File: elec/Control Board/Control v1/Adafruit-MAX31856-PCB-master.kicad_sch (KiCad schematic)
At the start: 23 parts, among them U1 mic5225-3.3, U2 MAX31856, X1 3.5mm term

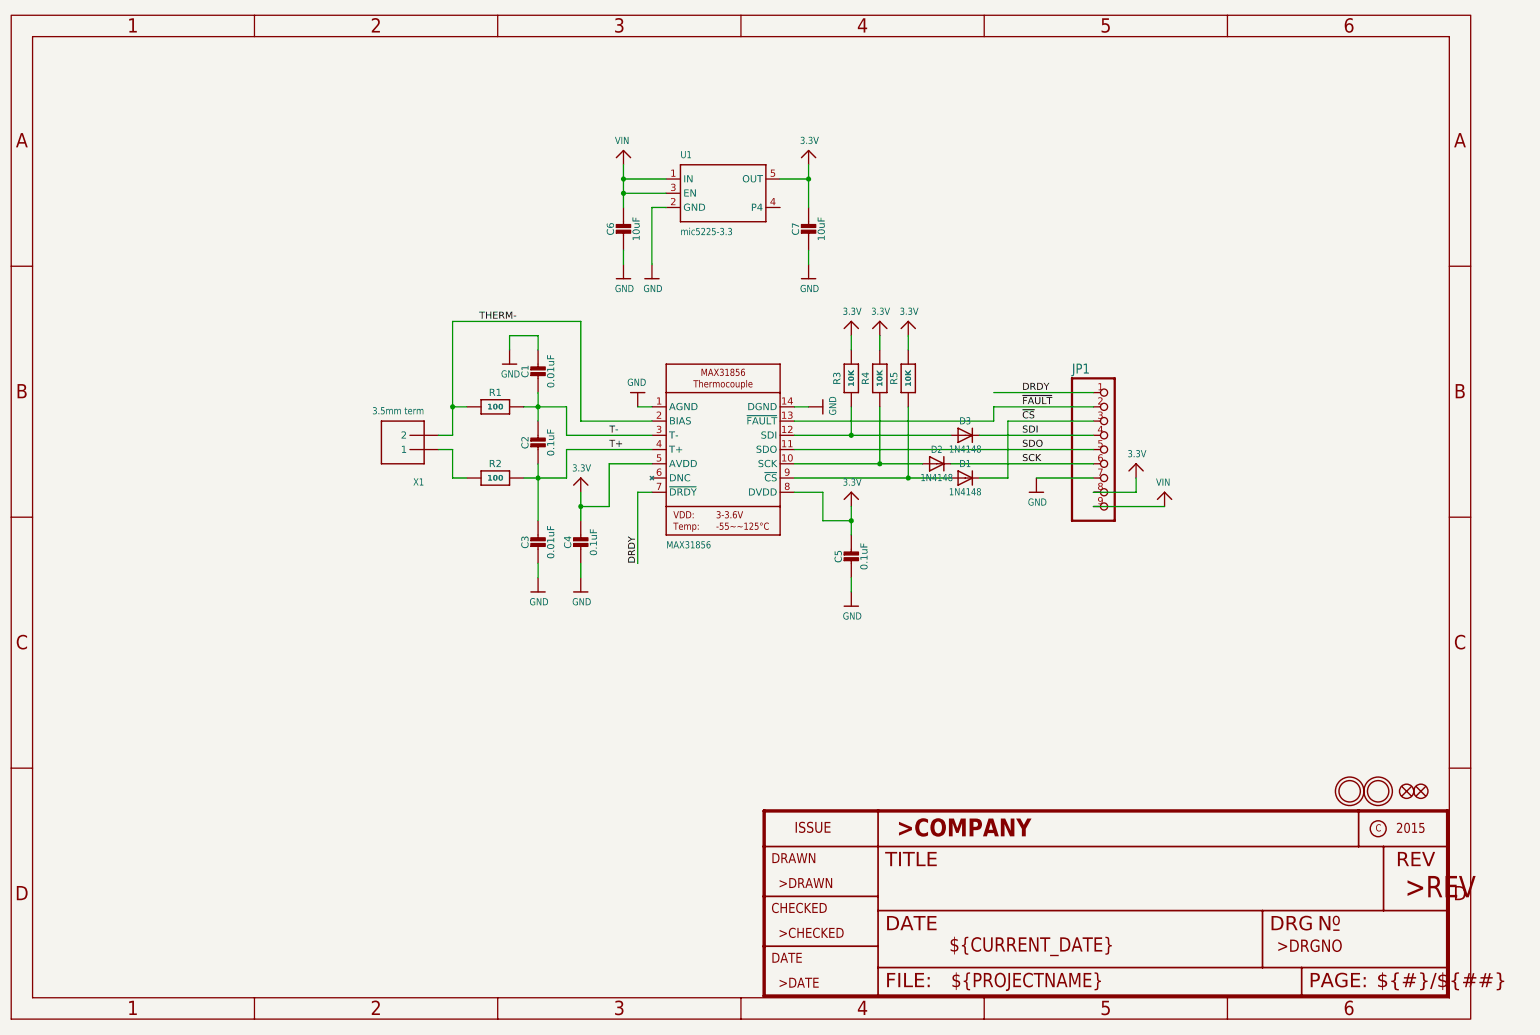
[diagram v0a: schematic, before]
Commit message: added labels for heiarchy sheets, and first pass on basic control interface circuits
Signed-off-by: lokimetasmith <lokimail@gmail.com>
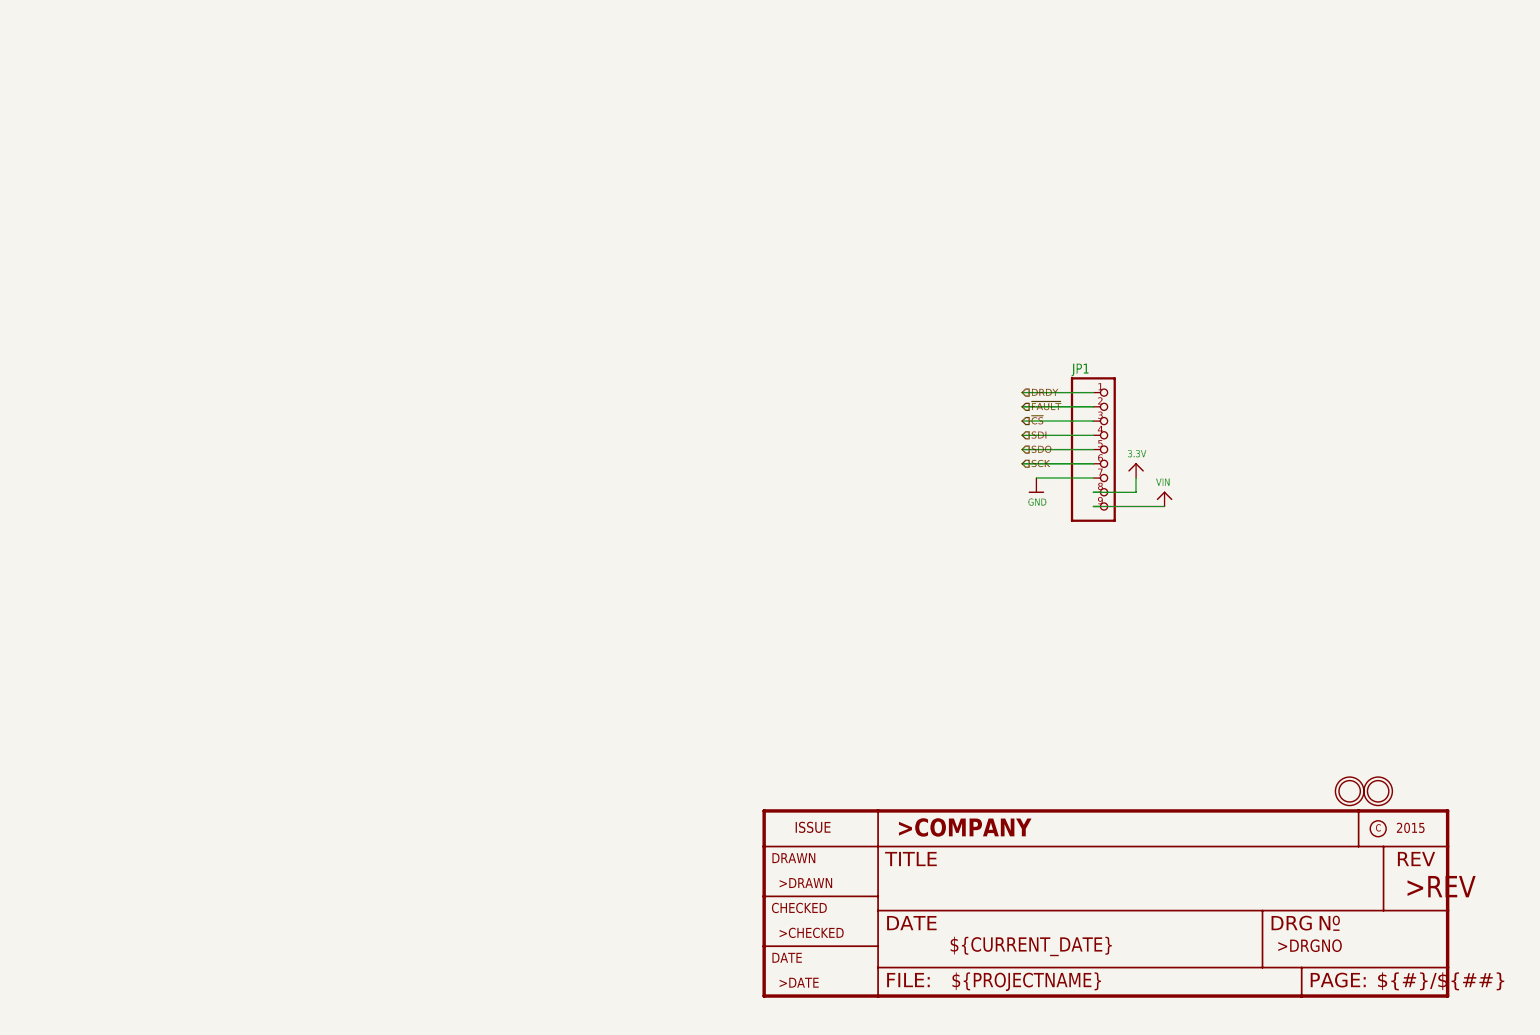
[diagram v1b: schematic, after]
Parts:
- removed C1: 0.01uF, Control v1:0805_10MGAP, symbol Control v1-eagle-import:microbuilder_CAP_CERAMIC0805_10MGAP
- removed C2, C4, C5: 0.1uF, Control v1:0805-NO, symbol Control v1-eagle-import:microbuilder_CAP_CERAMIC0805-NOOUTLINE
- removed C3: 0.01uF, Control v1:0805-NO, symbol Control v1-eagle-import:microbuilder_CAP_CERAMIC0805-NOOUTLINE
- removed C6, C7: 10uF, Control v1:0805-NO, symbol Control v1-eagle-import:microbuilder_CAP_CERAMIC0805-NOOUTLINE
- removed D1, D2, D3: 1N4148, Control v1:SOD-323, symbol Control v1-eagle-import:DIODESOD-323
- removed FID1, FID2: FIDUCIAL{dblquote}{dblquote}, Control v1:FIDUCIAL_1MM, symbol Control v1-eagle-import:microbuilder_FIDUCIAL{dblquote}{dblquote}
- removed R1, R2: 100, Control v1:0805-NO, symbol Control v1-eagle-import:RESISTOR0805_NOOUTLINE
- removed R3, R4, R5: 10K, Control v1:0805-NO, symbol Control v1-eagle-import:RESISTOR0805_NOOUTLINE
- removed U1: mic5225-3.3, Control v1:SOT23-5, symbol Control v1-eagle-import:microbuilder_VREG_SOT23-5
- removed U2: MAX31856, Control v1:TSSOP14, symbol Control v1-eagle-import:MAX31856
- removed X1: 3.5mm term, Control v1:TERMBLOCK_1X2-3.5MM, symbol Control v1-eagle-import:microbuilder_TERMBLOCK_1X2

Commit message: Add fan circuits. Add thermocouple interface circuits.
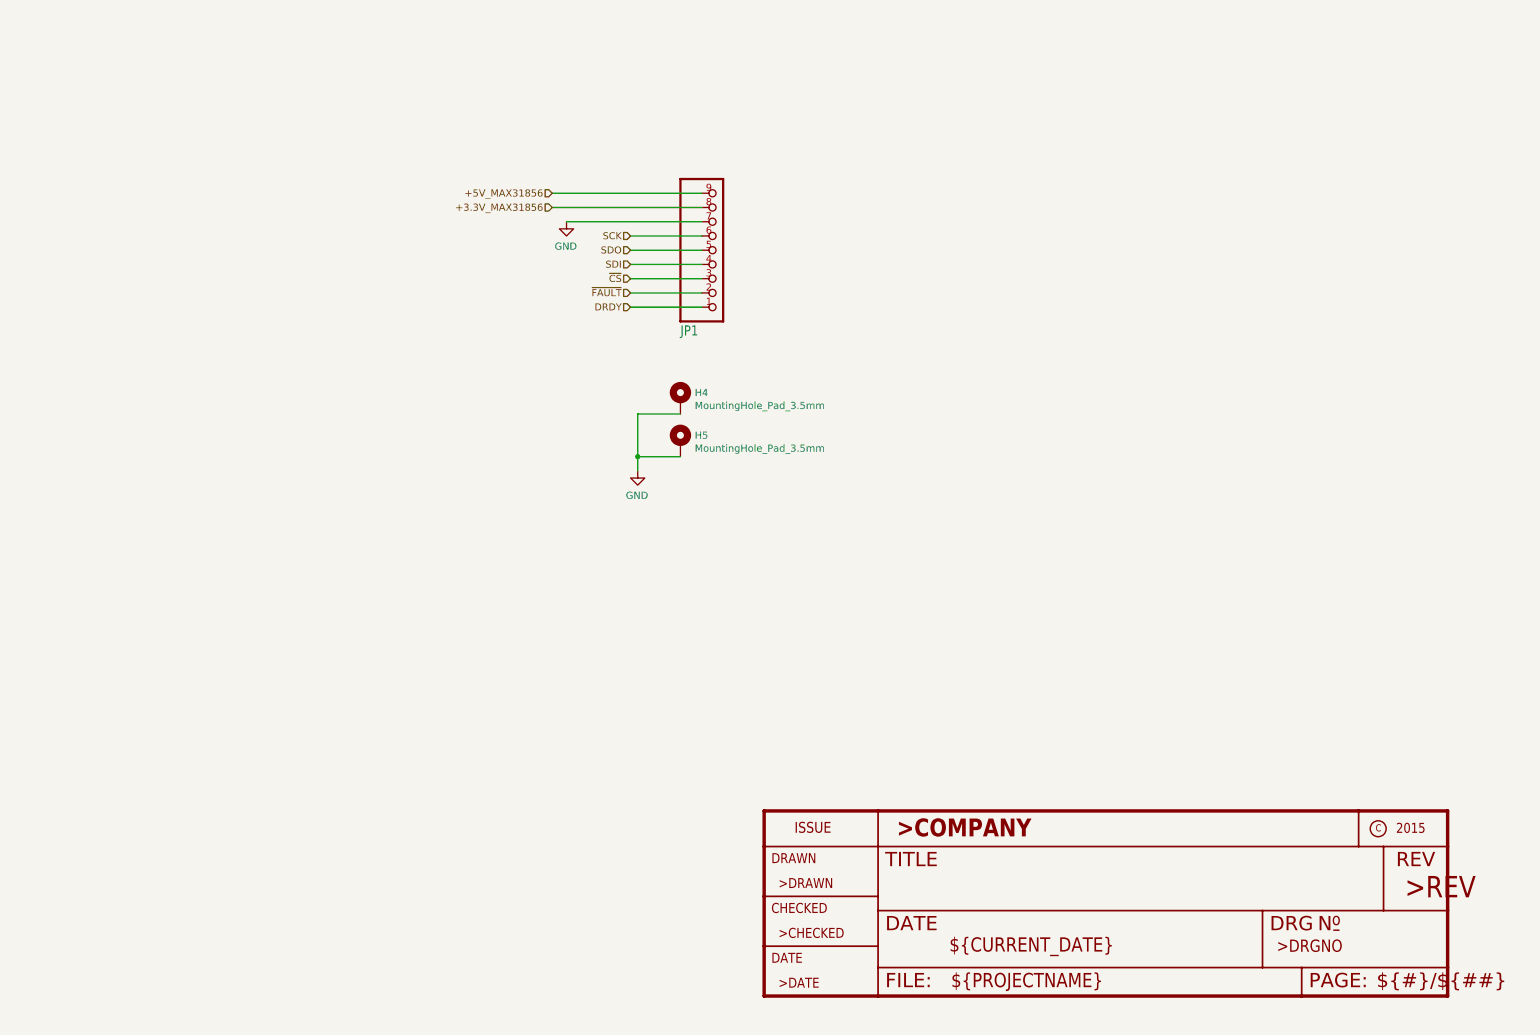
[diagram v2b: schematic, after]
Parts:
- removed U$13, U$14: MOUNTINGHOLE2.5, Control v1:MOUNTINGHOLE_2.5_PLATED, symbol Control v1-eagle-import:microbuilder_MOUNTINGHOLE2.5
- added H4, H5: MountingHole_Pad_3.5mm, GeneralPurposeAlarmDevicePCB:MountingHole_3.5mm_Pad_Via, symbol GPAD_SCH_LIB:MountingHole_Pad_3.5mm
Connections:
- net GND: now also H4.1, H5.1
- net 3.3V renamed +3.3V_MAX31856
- net VIN renamed +5V_MAX31856
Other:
- moved on the sheet: JP1

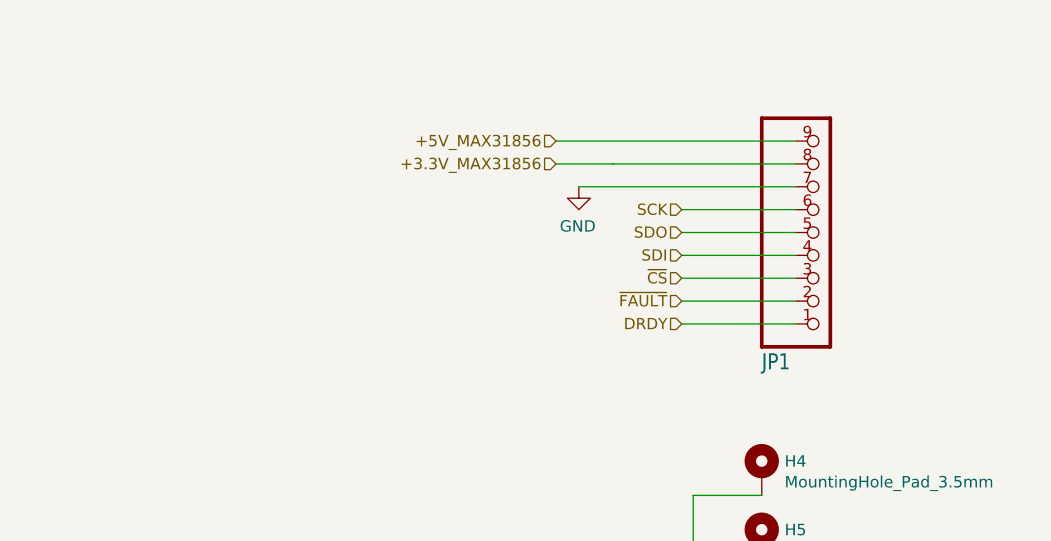
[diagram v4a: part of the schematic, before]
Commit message: Add footprints for thermoucouple modules to schematic and PCB.  This commit does NOT capture the library changes.
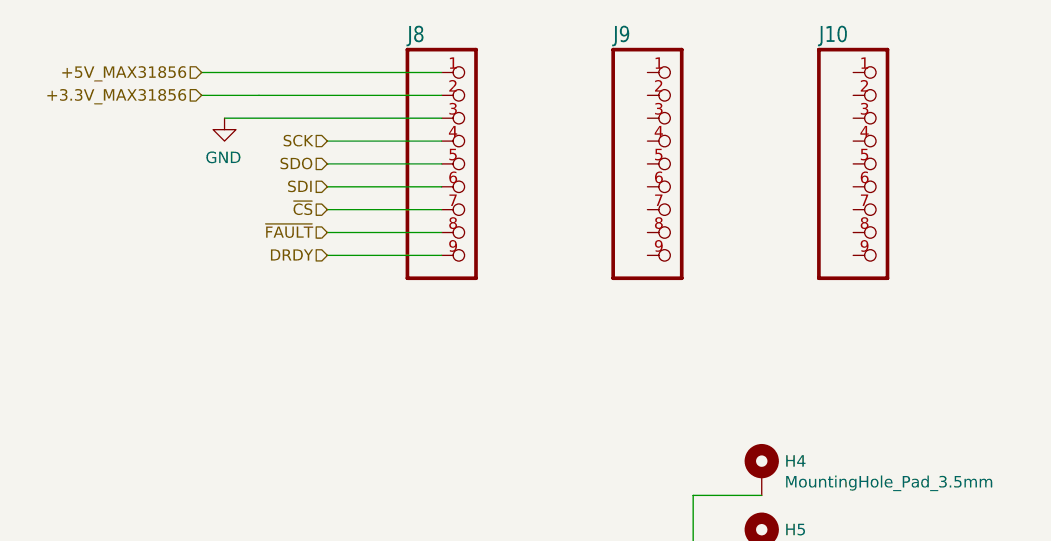
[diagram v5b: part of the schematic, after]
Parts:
- removed JP1: HEADER-1X970MIL, Control v1:1X09_ROUND_70, symbol Control v1-eagle-import:HEADER-1X970MIL
- added J10, J8, J9: MAX31865, PubInv_KiCad_PCB:Adafruit_MAX31865_Module, symbol Control v1-eagle-import:HEADER-1X970MIL
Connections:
- net +3.3V_MAX31856: now also J8.2
- net +5V_MAX31856: now also J8.1
- net DRDY: now also J8.9
- net GND: now also J8.3
- net SCK: now also J8.4
- net SDI: now also J8.6
- net SDO: now also J8.5
- net ~{CS}: now also J8.7
- net ~{FAULT}: now also J8.8

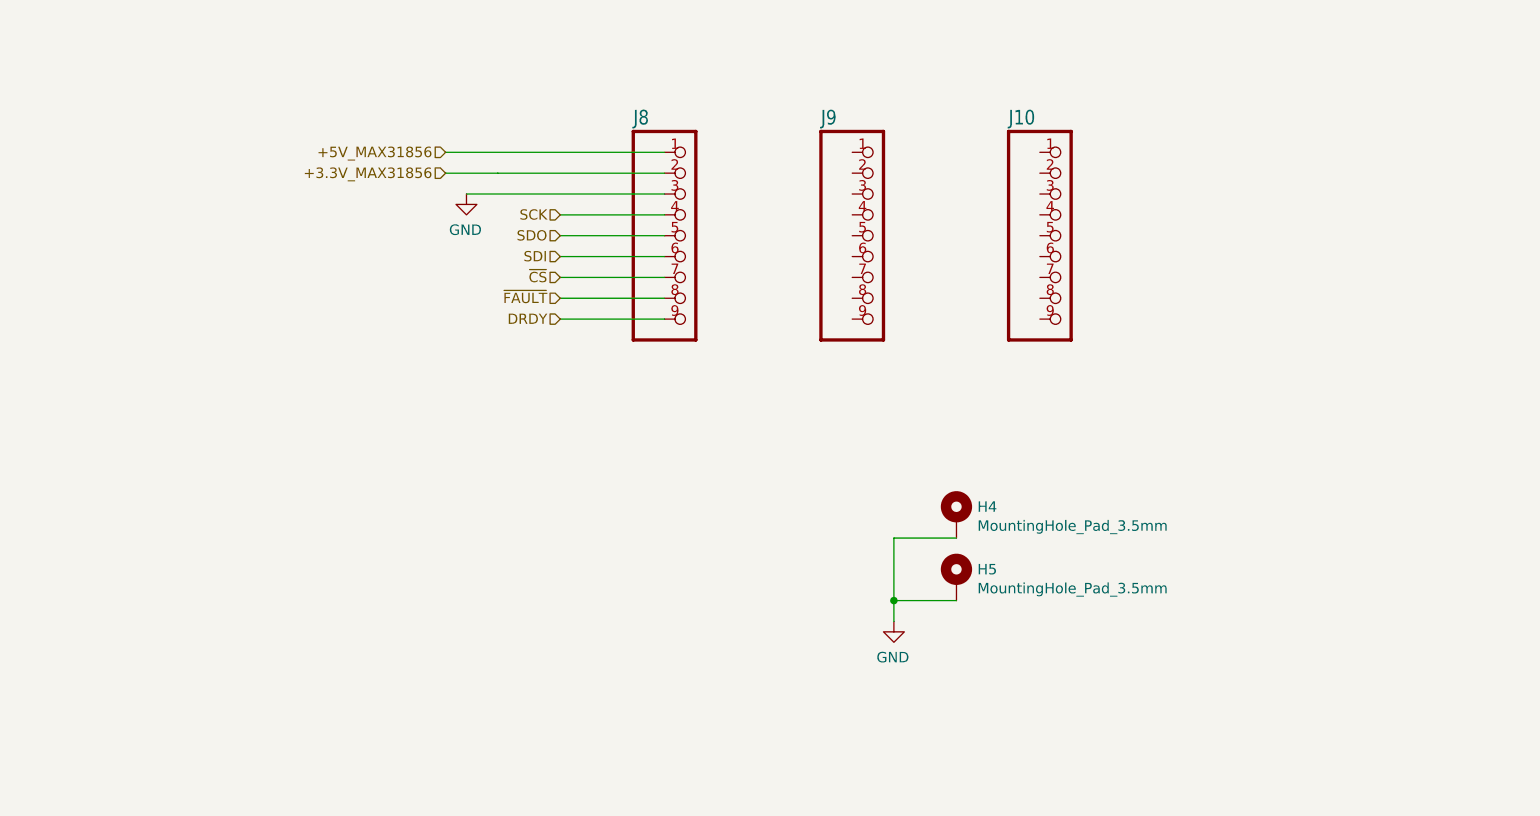
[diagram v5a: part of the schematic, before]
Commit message: Update schematic for MCP9600 I2C thermocouple.
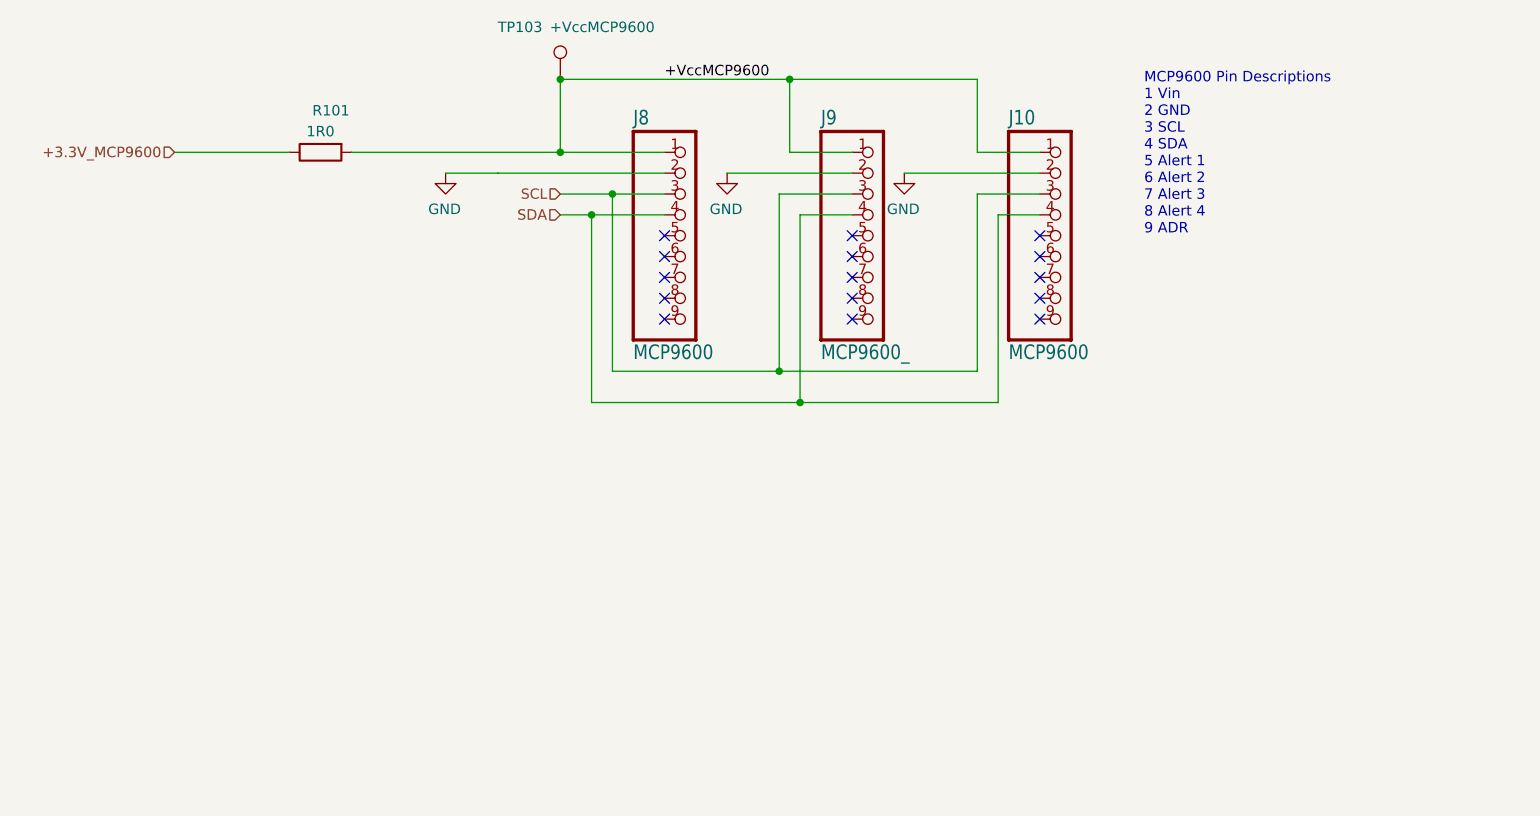
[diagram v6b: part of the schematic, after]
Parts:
- removed H4, H5: MountingHole_Pad_3.5mm, GeneralPurposeAlarmDevicePCB:MountingHole_3.5mm_Pad_Via, symbol GPAD_SCH_LIB:MountingHole_Pad_3.5mm
- added R101: 1R0, Resistor_SMD:R_0603_1608Metric_Pad0.98x0.95mm_HandSolder, symbol Device:R
- added TP103: +VccMCP9600, TestPoint:TestPoint_Loop_D2.54mm_Drill1.5mm_Beaded, symbol Connector:TestPoint
- J10, J8: value MAX31865 -> MCP9600; footprint PubInv_KiCad_PCB:Adafruit_MAX31865_Module -> PubInv_KiCad_PCB:Adafruit_MCP9600_Module
- J9: value MAX31865 -> MCP9600_; footprint PubInv_KiCad_PCB:Adafruit_MAX31865_Module -> PubInv_KiCad_PCB:Adafruit_MCP9600_Module
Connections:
- net +3.3V_MAX31856 is gone; now on net GND: J8.2
- net +5V_MAX31856 is gone; now on net +VccMCP9600: J8.1
- net SCK is gone; now on net SDA: J8.4
- net GND: now also J10.2, J9.2; no longer J8.3
- net +VccMCP9600: now reaches J10.1
- net +VccMCP9600: now also J9.1, R101.2, TP103.1
- net SCL: now reaches J10.3
- net SCL: now also J8.3, J9.3
- net SDA: now reaches J10.4
- net SDA: now also J9.4
- net DRDY: no longer names the net of J8.9
- net SDI: no longer names the net of J8.6
- net SDO: no longer names the net of J8.5
- net ~{CS}: no longer names the net of J8.7
- net ~{FAULT}: no longer names the net of J8.8
- new net +3.3V_MCP9600: R101.1
- no-connect marks 0 -> 15
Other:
- note added: "MCP9600 Pin Descriptions 1 Vin 2 GND 3 SCL 4 SDA 5 Alert 1 6 Alert 2 7 Alert 3 8 Alert 4 9 ADR"
